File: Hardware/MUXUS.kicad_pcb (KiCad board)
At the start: 4 copper layers, 99.1 x 99.1 mm, 119 parts, among them J1 USB_C_Receptacle_USB2.0, J2 USB_B, J3 USB_A, J4 USB_B, J5 USB_A, J6 STDC14, J7 USB_B, J8 USB_A, SW1 USER, SW2 RESET, U1 USBLC6-4SC6, U10 AP2151W, U11 AOZ1212AI, U12 USBLC6-2SC6, U13 USBLC6-2SC6, U14 AP2151W, U2 USB2504A-JT, U3 USBLC6-2SC6, U4 USBLC6-2SC6, U5 AP2151W, U6 TS3USBCA420RSVR, U7 STM32G431K8T6, U8 USBLC6-2SC6, U9 USBLC6-2SC6, Y1 ATS240C

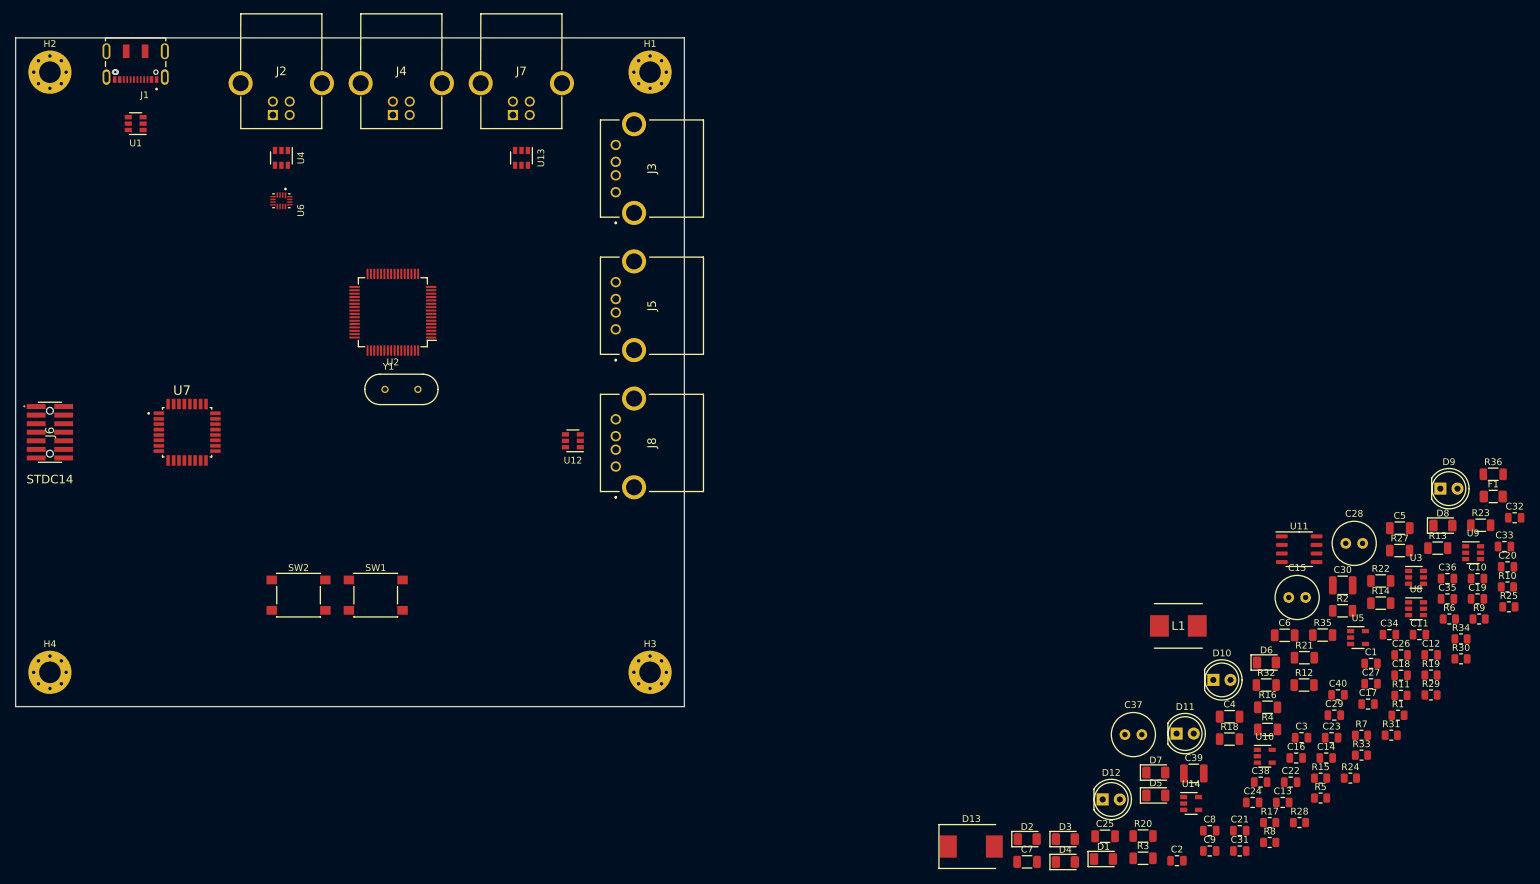
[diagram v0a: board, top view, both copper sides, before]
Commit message: LED positioning
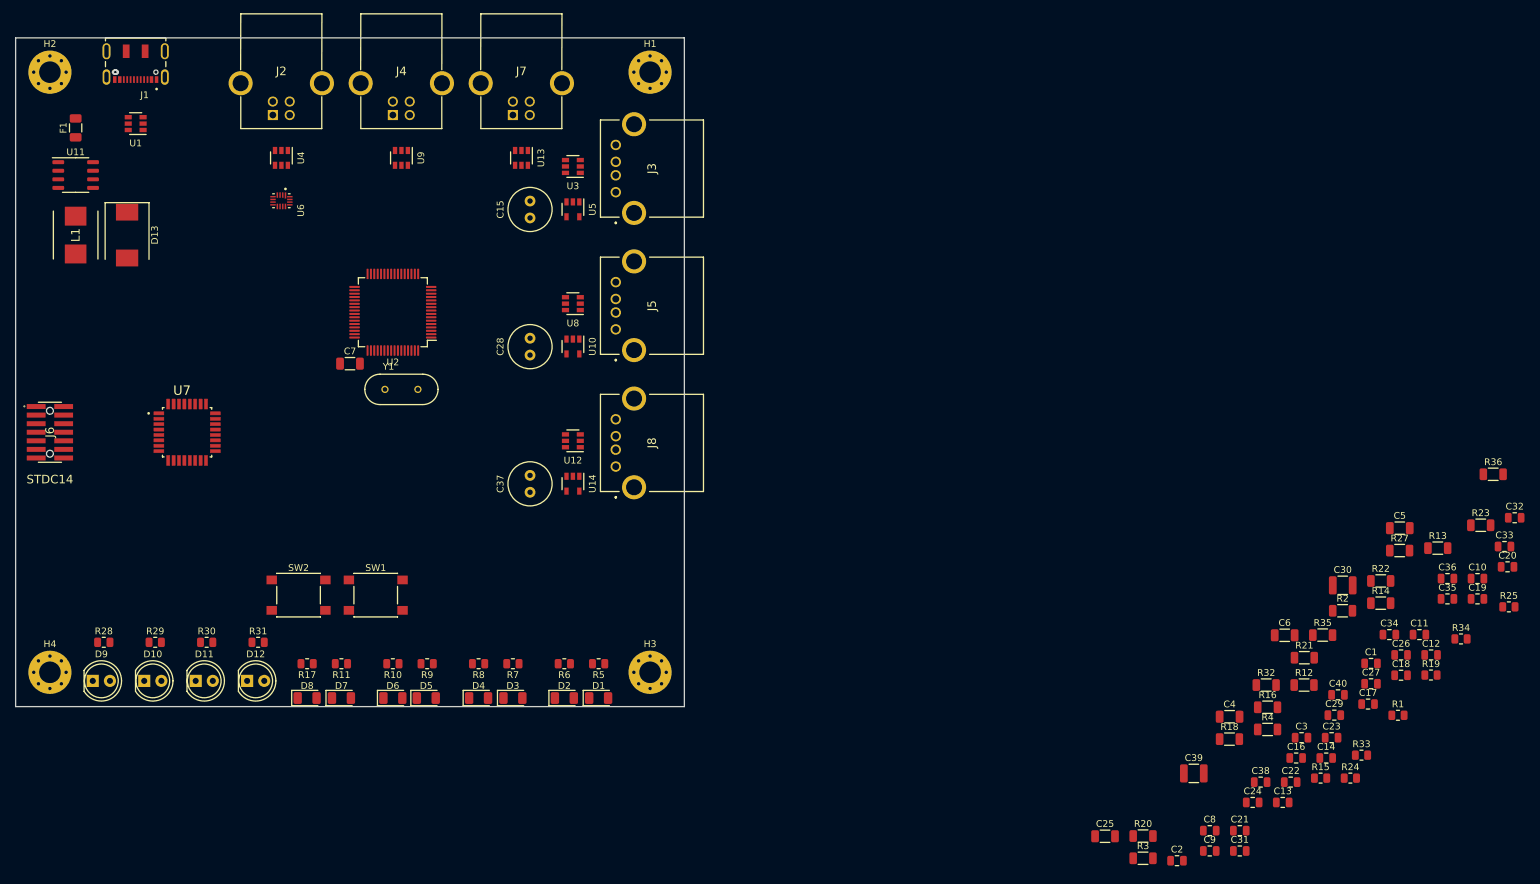
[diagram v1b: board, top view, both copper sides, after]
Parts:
- moved F1 217.0 mm to (24.1, 28.6), turned to 90 degrees
- moved D9 201.6 mm to (26.7, 110.5)
- moved U11 189.5 mm to (24.1, 35.6)
- moved R29 189.1 mm to (35.9, 104.8)
- moved R30 185.8 mm to (43.5, 104.8)
- moved R28 179.1 mm to (28.3, 104.8)
- moved L1 173.3 mm to (24.1, 44.5), turned to 270 degrees
- moved D8 170.2 mm to (58.4, 113.0)
- moved U9 169.2 mm to (72.4, 33.0), turned to 270 degrees
- moved R31 168.4 mm to (51.2, 104.8)
- moved R10 165.5 mm to (71.1, 108.0), turned to 180 degrees
- moved D10 158.4 mm to (34.3, 110.5)
- moved R11 157.0 mm to (63.5, 108.0), turned to 180 degrees
- moved R9 156.0 mm to (76.2, 108.0), turned to 180 degrees
- moved D13 154.4 mm to (31.8, 44.5), turned to 270 degrees
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
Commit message: More footprint positioning
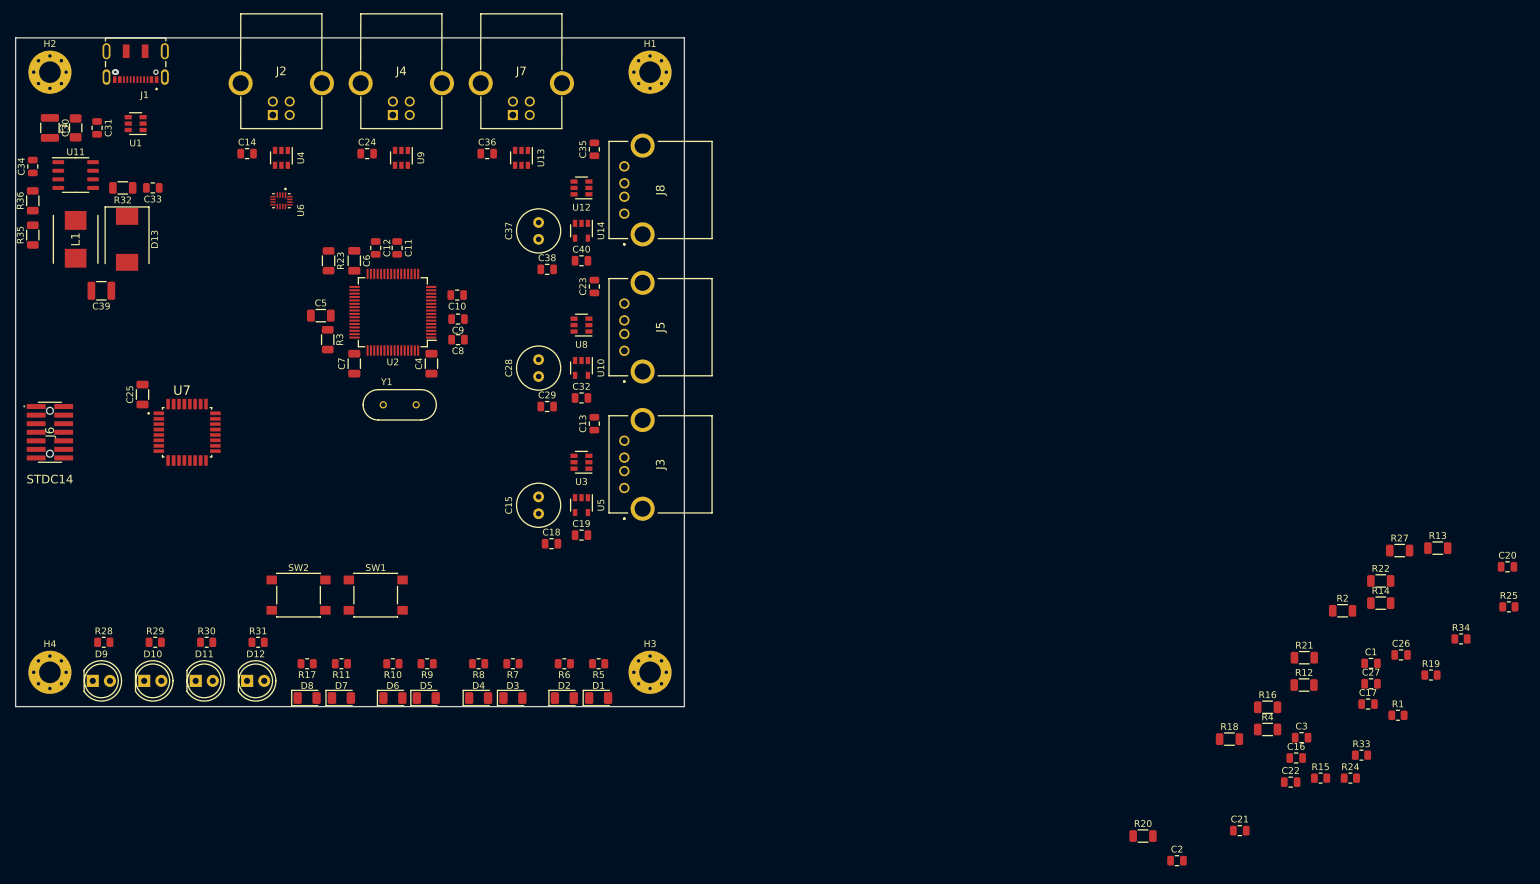
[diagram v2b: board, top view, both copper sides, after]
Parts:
- moved R36 220.1 mm to (17.8, 39.4), turned to 90 degrees
- moved C34 212.6 mm to (17.8, 34.3), turned to 90 degrees
- moved C33 207.2 mm to (35.6, 37.5), turned to 180 degrees
- moved C30 203.1 mm to (20.3, 28.6), turned to 270 degrees
- moved C31 200.3 mm to (27.3, 28.6), turned to 270 degrees
- moved R35 200.1 mm to (17.8, 44.5), turned to 90 degrees
- moved R32 184.7 mm to (31.1, 37.5), turned to 180 degrees
- moved C14 183.2 mm to (49.5, 32.4)
- moved C39 176.9 mm to (27.9, 52.7), turned to 180 degrees
- moved R23 175.1 mm to (61.6, 48.3), turned to 270 degrees
- moved C12 167.6 mm to (68.6, 46.4), turned to 270 degrees
- moved C5 162.9 mm to (60.5, 56.4)
- moved C24 162.6 mm to (67.3, 32.4)
- moved C11 161.9 mm to (71.8, 46.4), turned to 270 degrees
- moved C25 156.9 mm to (34.0, 68.1), turned to 90 degrees
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
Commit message: AMOGUS and USB C footprint update
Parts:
- added SYM1: AMOGUS, AMOGUS:SUS, F.Cu at (107.3, 95.2)

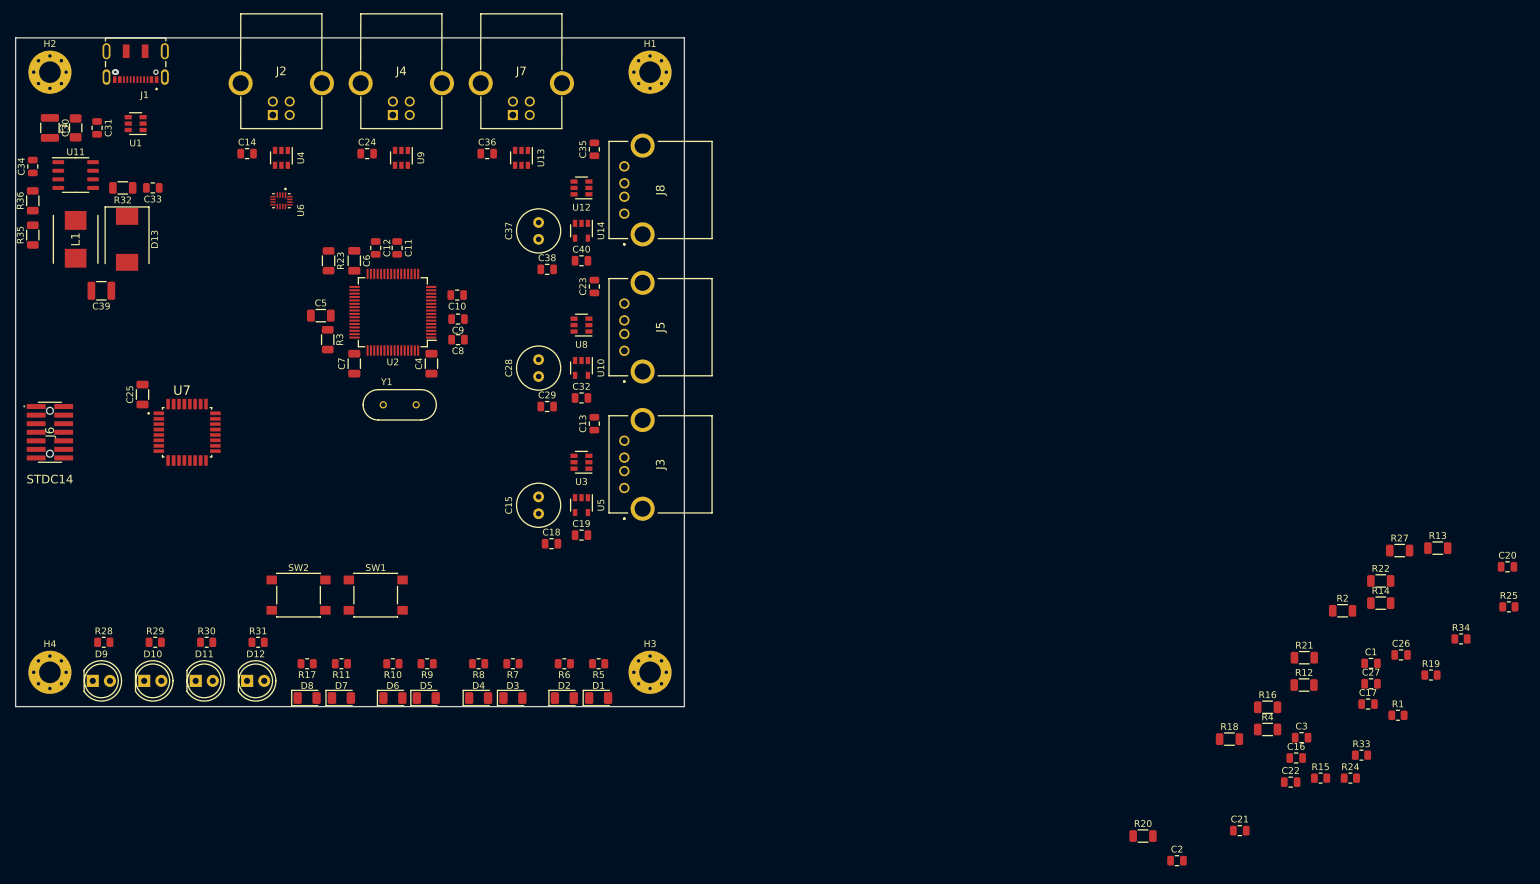
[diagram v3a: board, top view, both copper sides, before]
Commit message: Component placement finished
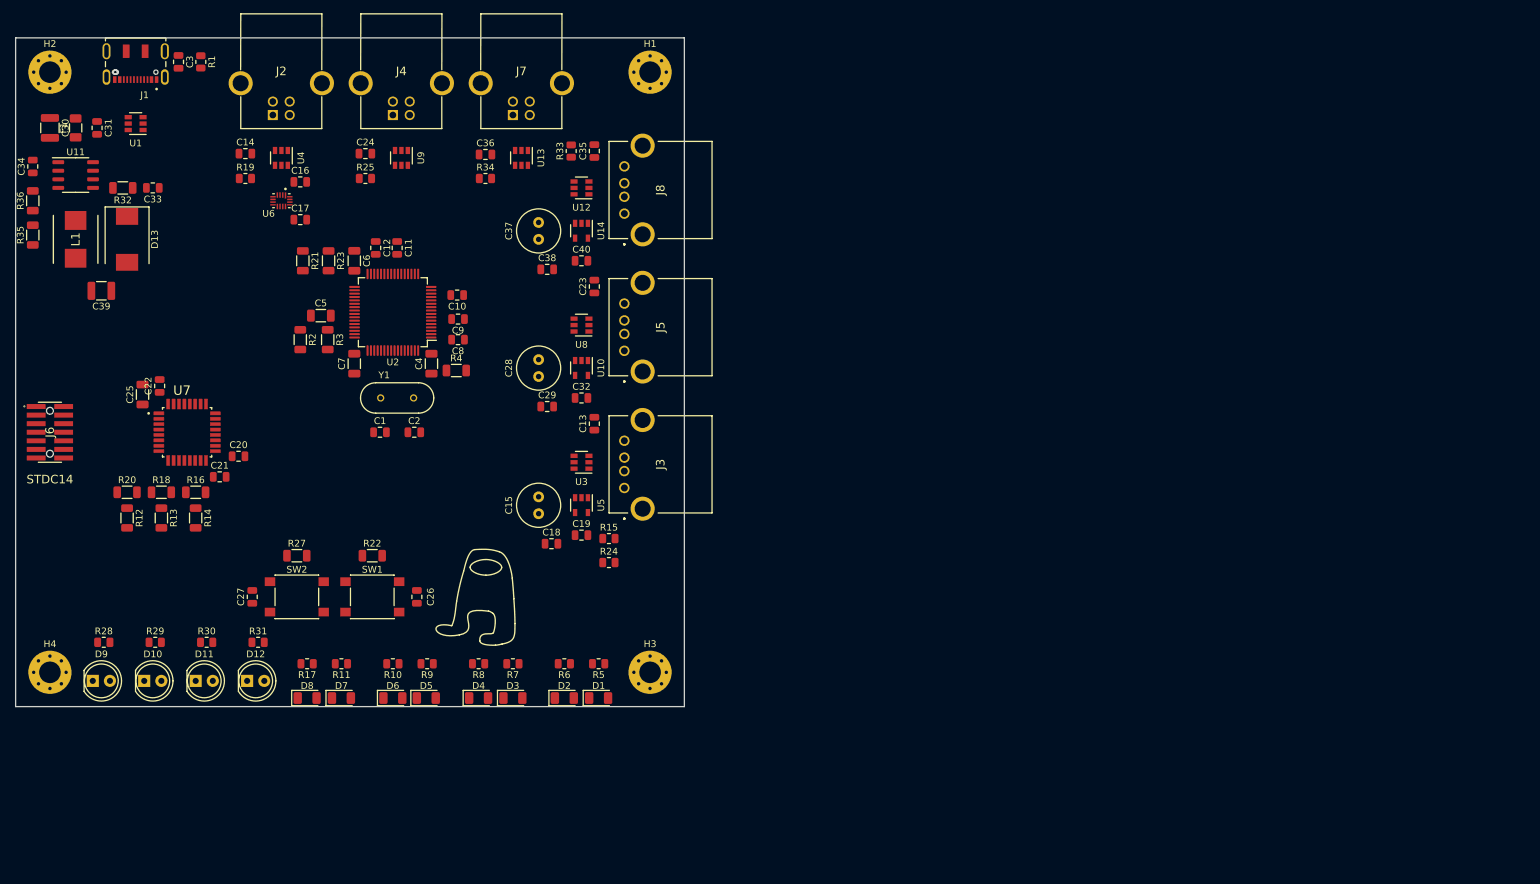
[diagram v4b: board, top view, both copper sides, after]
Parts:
- moved R1 202.0 mm to (42.7, 18.8), turned to 270 degrees
- moved C3 194.2 mm to (39.4, 18.8), turned to 270 degrees
- moved R19 190.4 mm to (49.3, 36.1)
- moved R13 189.1 mm to (36.8, 86.4), turned to 270 degrees
- moved C20 188.7 mm to (48.3, 77.2)
- moved R25 180.9 mm to (67.1, 36.1)
- moved C22 177.5 mm to (36.6, 66.8), turned to 90 degrees
- moved R12 176.1 mm to (31.8, 86.4), turned to 270 degrees
- moved R14 176.0 mm to (41.9, 86.4), turned to 270 degrees
- moved C17 173.7 mm to (57.4, 42.2)
- moved C16 170.4 mm to (57.4, 36.6)
- moved C27 166.2 mm to (50.3, 98.0), turned to 90 degrees
- moved R27 163.4 mm to (56.9, 91.9)
- moved R18 162.4 mm to (36.8, 82.5)
- moved R16 161.9 mm to (41.9, 82.5)
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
